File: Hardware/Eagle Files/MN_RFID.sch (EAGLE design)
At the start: 23 parts, among them IC1 74HCT125N, J1 USB_B_PTH, U1 ARGON

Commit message: Updated Schematic
Updated schematic per testing breadboard at MN 8/07/19.  Decided to power from Argon and remove external 5v USB connector, 3.3v power converter, and 100 uF cap.  5v supplied from Argon via VUSB pin.  3.3v supplied from Argon via 3.3v pin.  Also added 5.6Kohm pulldown on D4 to prevent buzzer from going off while Argon sets up.
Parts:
- removed C3: 100uF, adafruit:CPOL-USE2.5-5
- removed J1: USB_B_PTH, SparkFun-Connectors:USB_B_PTH
- removed PWR: (no value), adafruit:PINHD-1X3
- added R7: 5.6k, adafruit:R-US_0204/7
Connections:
- removed net N$19: IC1A.I, U1.D2
- new net N$22: IC1A.I, R7.1, U1.D2
- net 3.3V: no longer PWR.2
- net 5V: now also U1.VUSB; no longer C3.+, J1.VBUS, PWR.1
- net GND: now also R7.2; no longer C3.-, J1.GND, J1.SHIELD, PWR.3
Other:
- note added: "N/C"
- note removed: "OUT"
- note removed: "VIN"

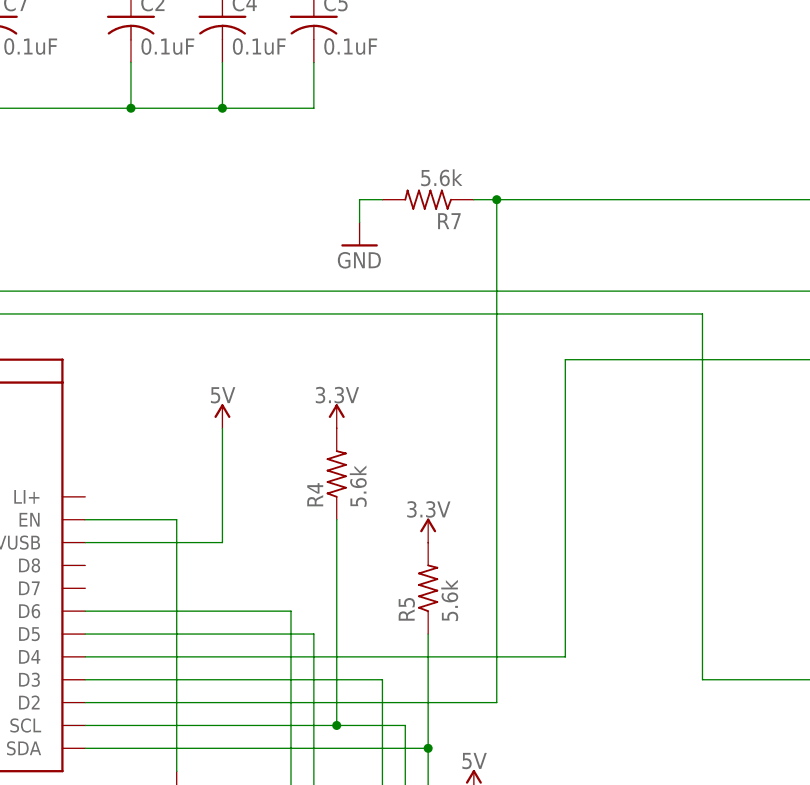
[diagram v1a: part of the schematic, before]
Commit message: Updated schematic
Changed pull-up/down resistors from 5.6K to 4.7K -- more common value.
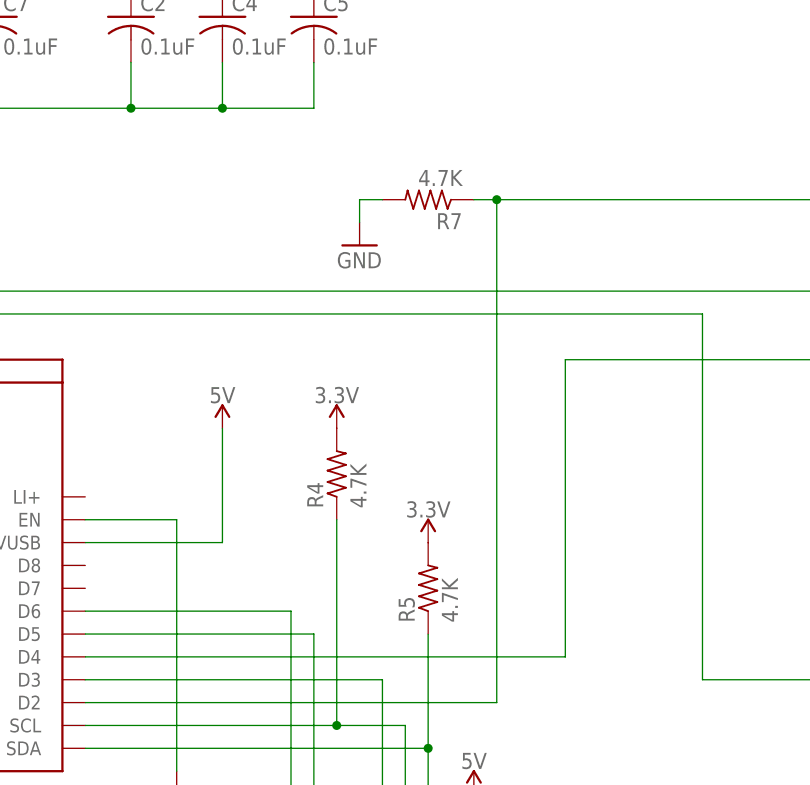
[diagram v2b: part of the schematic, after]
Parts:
- R4, R5, R7: value 5.6k -> 4.7K
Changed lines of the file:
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@@
 <part name="SUPPLY7" library="SparkFun-PowerSymbols" library_urn="urn:adsk.eagle:library:530" deviceset="5V" device=""/>
 <part name="GND9" library="supply1" library_urn="urn:adsk.eagle:library:371" deviceset="GND" device=""/>
-<part name="R4" library="adafruit" library_urn="urn:adsk.eagle:library:420" deviceset="R-US_" device="0204/7" package3d_urn="urn:adsk.eagle:package:6240596/1" value="5.6k"/>
-<part name="R5" library="adafruit" library_urn="urn:adsk.eagle:library:420" deviceset="R-US_" device="0204/7" package3d_urn="urn:adsk.eagle:package:6240596/1" value="5.6k"/>
+<part name="R4" library="adafruit" library_urn="urn:adsk.eagle:library:420" deviceset="R-US_" device="0204/7" package3d_urn="urn:adsk.eagle:package:6240596/1" value="4.7K"/>
+<part name="R5" library="adafruit" library_urn="urn:adsk.eagle:library:420" deviceset="R-US_" device="0204/7" package3d_urn="urn:adsk.eagle:package:6240596/1" value="4.7K"/>
 <part name="SUPPLY6" library="SparkFun-PowerSymbols" library_urn="urn:adsk.eagle:library:530" deviceset="3.3V" device=""/>
 <part name="SUPPLY8" library="SparkFun-PowerSymbols" library_urn="urn:adsk.eagle:library:530" deviceset="3.3V" device=""/>
@@
 <part name="C7" library="adafruit" library_urn="urn:adsk.eagle:library:420" deviceset="C-US" device="025-024X044" package3d_urn="urn:adsk.eagle:package:6240324/1" value="0.1uF"/>
 <part name="SUPPLY11" library="SparkFun-PowerSymbols" library_urn="urn:adsk.eagle:library:530" deviceset="5V" device=""/>
-<part name="R7" library="adafruit" library_urn="urn:adsk.eagle:library:420" deviceset="R-US_" device="0204/7" package3d_urn="urn:adsk.eagle:package:6240596/1" value="5.6k"/>
+<part name="R7" library="adafruit" library_urn="urn:adsk.eagle:library:420" deviceset="R-US_" device="0204/7" package3d_urn="urn:adsk.eagle:package:6240596/1" value="4.7K"/>
 <part name="GND11" library="supply1" library_urn="urn:adsk.eagle:library:371" deviceset="GND" device=""/>
 </parts>

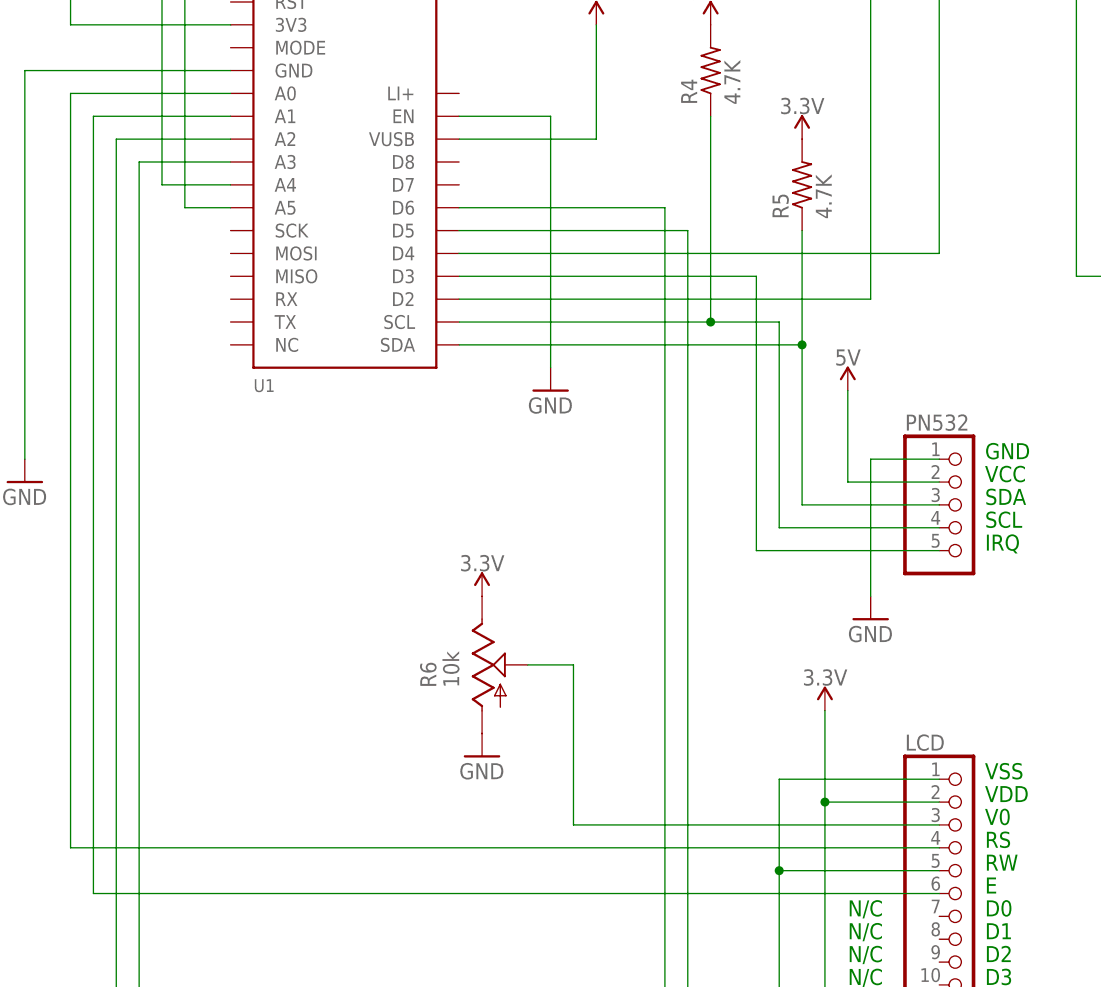
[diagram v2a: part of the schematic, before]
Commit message: PCB Finalization
Added expansion connector and board name.  Routed and coppoer pour.  Annotated the top silkscreen layer for connection information.
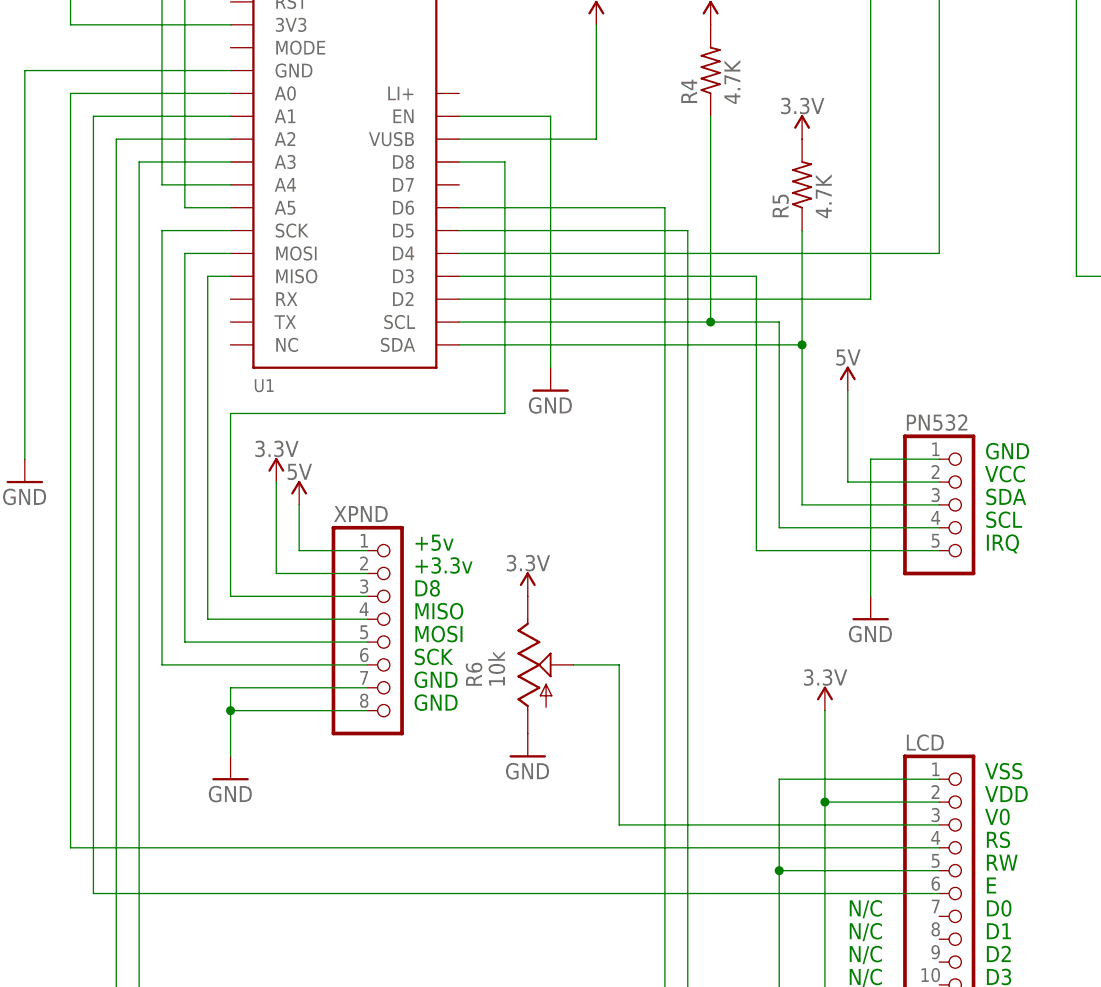
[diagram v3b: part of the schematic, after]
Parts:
- added XPND: (no value), adafruit:PINHD-1X8BIG
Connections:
- new net N$19: U1.D8, XPND.3
- new net N$23: U1.MISO, XPND.4
- new net N$24: U1.MOSI, XPND.5
- new net N$25: U1.SCK, XPND.6
- net 3.3V: now also XPND.2
- net 5V: now also XPND.1
- net GND: now also XPND.7, XPND.8
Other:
- note added: "+3.3v"
- note added: "+5v"
- note added: "D8"
- note added: "MISO"
- note added: "MOSI"
- note added: "SCK"
- moved on the sheet: R6
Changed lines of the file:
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@@
 <part name="R7" library="adafruit" library_urn="urn:adsk.eagle:library:420" deviceset="R-US_" device="0204/7" package3d_urn="urn:adsk.eagle:package:6240596/1" value="4.7K"/>
 <part name="GND11" library="supply1" library_urn="urn:adsk.eagle:library:371" deviceset="GND" device=""/>
+<part name="XPND" library="adafruit" library_urn="urn:adsk.eagle:library:420" deviceset="PINHD-1X8" device="BIG" package3d_urn="urn:adsk.eagle:package:6240707/1"/>
+<part name="SUPPLY10" library="SparkFun-PowerSymbols" library_urn="urn:adsk.eagle:library:530" deviceset="5V" device=""/>
+<part name="SUPPLY12" library="SparkFun-PowerSymbols" library_urn="urn:adsk.eagle:library:530" deviceset="3.3V" device=""/>
+<part name="GND12" library="supply1" library_urn="urn:adsk.eagle:library:371" deviceset="GND" device=""/>
 </parts>
 <sheets>
@@
 <text x="-38.1" y="15.24" size="1.778" layer="91">N/C</text>
 <text x="-38.1" y="12.7" size="1.778" layer="91">N/C</text>
+<text x="-86.36" y="60.96" size="1.778" layer="91">+5v</text>
+<text x="-86.36" y="58.42" size="1.778" layer="91">+3.3v</text>
+<text x="-86.36" y="55.88" size="1.778" layer="91">D8</text>
+<text x="-86.36" y="53.34" size="1.778" layer="91">MISO</text>
+<text x="-86.36" y="50.8" size="1.778" layer="91">MOSI</text>
+<text x="-86.36" y="48.26" size="1.778" layer="91">SCK</text>
+<text x="-86.36" y="45.72" size="1.778" layer="91">GND</text>
+<text x="-86.36" y="43.18" size="1.778" layer="91">GND</text>
 </plain>
 <instances>
@@
 <attribute name="VALUE" x="-100.584" y="160.909" size="1.778" layer="96"/>
 </instance>
-<instance part="R6" gate="G$1" x="-78.74" y="48.26" smashed="yes">
-<attribute name="NAME" x="-83.82" y="45.72" size="1.778" layer="95" rot="R90"/>
-<attribute name="VALUE" x="-81.28" y="45.72" size="1.778" layer="96" rot="R90"/>
-</instance>
-<instance part="GND10" gate="1" x="-78.74" y="38.1" smashed="yes">
-<attribute name="VALUE" x="-81.28" y="35.56" size="1.778" layer="96"/>
-</instance>
-<instance part="SUPPLY9" gate="G$1" x="-78.74" y="55.88" smashed="yes">
-<attribute name="VALUE" x="-78.74" y="58.674" size="1.778" layer="96" align="bottom-center"/>
+<instance part="R6" gate="G$1" x="-73.66" y="48.26" smashed="yes">
+<attribute name="NAME" x="-78.74" y="45.72" size="1.778" layer="95" rot="R90"/>
+<attribute name="VALUE" x="-76.2" y="45.72" size="1.778" layer="96" rot="R90"/>
+</instance>
+<instance part="GND10" gate="1" x="-73.66" y="38.1" smashed="yes">
+<attribute name="VALUE" x="-76.2" y="35.56" size="1.778" layer="96"/>
+</instance>
+<instance part="SUPPLY9" gate="G$1" x="-73.66" y="55.88" smashed="yes">
+<attribute name="VALUE" x="-73.66" y="58.674" size="1.778" layer="96" align="bottom-center"/>
 </instance>
 <instance part="C7" gate="G$1" x="-91.44" y="165.1" smashed="yes">
@@
 <instance part="GND11" gate="1" x="-50.8" y="139.7" smashed="yes">
 <attribute name="VALUE" x="-53.34" y="137.16" size="1.778" layer="96"/>
+</instance>
+<instance part="XPND" gate="G$1" x="-88.9" y="53.34" smashed="yes">
+<attribute name="NAME" x="-95.25" y="64.135" size="1.778" layer="95"/>
+<attribute name="VALUE" x="-95.25" y="38.1" size="1.778" layer="96"/>
+</instance>
+<instance part="SUPPLY10" gate="G$1" x="-99.06" y="66.04" smashed="yes">
+<attribute name="VALUE" x="-99.06" y="68.834" size="1.778" layer="96" align="bottom-center"/>
+</instance>
+<instance part="SUPPLY12" gate="G$1" x="-101.6" y="68.58" smashed="yes">
+<attribute name="VALUE" x="-101.6" y="71.374" size="1.778" layer="96" align="bottom-center"/>
+</instance>
+<instance part="GND12" gate="1" x="-106.68" y="35.56" smashed="yes">
+<attribute name="VALUE" x="-109.22" y="33.02" size="1.778" layer="96"/>
 </instance>
 </instances>
@@
 <wire x1="-50.8" y1="144.78" x2="-50.8" y2="142.24" width="0.1524" layer="91"/>
 </segment>
+<segment>
+<pinref part="XPND" gate="G$1" pin="7"/>
+<wire x1="-91.44" y1="45.72" x2="-106.68" y2="45.72" width="0.1524" layer="91"/>
+<pinref part="GND12" gate="1" pin="GND"/>
+<wire x1="-106.68" y1="45.72" x2="-106.68" y2="43.18" width="0.1524" layer="91"/>
+<pinref part="XPND" gate="G$1" pin="8"/>
+<wire x1="-106.68" y1="43.18" x2="-106.68" y2="38.1" width="0.1524" layer="91"/>
+<wire x1="-91.44" y1="43.18" x2="-106.68" y2="43.18" width="0.1524" layer="91"/>
+<junction x="-106.68" y="43.18"/>
+</segment>
 </net>
 <net name="N$1" class="0">
@@
 <wire x1="-66.04" y1="106.68" x2="-81.28" y2="106.68" width="0.1524" layer="91"/>
 </segment>
+<segment>
+<pinref part="SUPPLY10" gate="G$1" pin="5V"/>
+<wire x1="-99.06" y1="66.04" x2="-99.06" y2="60.96" width="0.1524" layer="91"/>
+<pinref part="XPND" gate="G$1" pin="1"/>
+<wire x1="-99.06" y1="60.96" x2="-91.44" y2="60.96" width="0.1524" layer="91"/>
+</segment>
 </net>
 <net name="3.3V" class="0">
@@
 <wire x1="-43.18" y1="175.26" x2="-43.18" y2="180.34" width="0.1524" layer="91"/>
 </segment>
+<segment>
+<pinref part="SUPPLY12" gate="G$1" pin="3.3V"/>
+<wire x1="-101.6" y1="68.58" x2="-101.6" y2="58.42" width="0.1524" layer="91"/>
+<pinref part="XPND" gate="G$1" pin="2"/>
+<wire x1="-101.6" y1="58.42" x2="-91.44" y2="58.42" width="0.1524" layer="91"/>
+</segment>
 </net>
 <net name="N$2" class="0">
@@
 <net name="N$17" class="0">
 <segment>
+<pinref part="LCD" gate="A" pin="3"/>
+<wire x1="-27.94" y1="30.48" x2="-63.5" y2="30.48" width="0.1524" layer="91"/>
 <pinref part="R6" gate="G$1" pin="S"/>
-<wire x1="-68.58" y1="30.48" x2="-68.58" y2="48.26" width="0.1524" layer="91"/>
-<wire x1="-68.58" y1="48.26" x2="-73.66" y2="48.26" width="0.1524" layer="91"/>
-<pinref part="LCD" gate="A" pin="3"/>
-<wire x1="-27.94" y1="30.48" x2="-68.58" y2="30.48" width="0.1524" layer="91"/>
+<wire x1="-68.58" y1="48.26" x2="-63.5" y2="48.26" width="0.1524" layer="91"/>
+<wire x1="-63.5" y1="48.26" x2="-63.5" y2="30.48" width="0.1524" layer="91"/>
 </segment>
 </net>
@@
 </segment>
 </net>
+<net name="N$19" class="0">
+<segment>
+<pinref part="U1" gate="U1" pin="D8"/>
+<wire x1="-81.28" y1="104.14" x2="-76.2" y2="104.14" width="0.1524" layer="91"/>
+<wire x1="-76.2" y1="104.14" x2="-76.2" y2="76.2" width="0.1524" layer="91"/>
+<wire x1="-76.2" y1="76.2" x2="-106.68" y2="76.2" width="0.1524" layer="91"/>
+<wire x1="-106.68" y1="76.2" x2="-106.68" y2="55.88" width="0.1524" layer="91"/>
+<pinref part="XPND" gate="G$1" pin="3"/>
+<wire x1="-106.68" y1="55.88" x2="-91.44" y2="55.88" width="0.1524" layer="91"/>
+</segment>
+</net>
+<net name="N$23" class="0">
+<segment>
+<pinref part="U1" gate="U1" pin="MISO"/>
+<wire x1="-106.68" y1="91.44" x2="-109.22" y2="91.44" width="0.1524" layer="91"/>
+<pinref part="XPND" gate="G$1" pin="4"/>
+<wire x1="-109.22" y1="91.44" x2="-109.22" y2="53.34" width="0.1524" layer="91"/>
+<wire x1="-109.22" y1="53.34" x2="-91.44" y2="53.34" width="0.1524" layer="91"/>
+</segment>
+</net>
+<net name="N$24" class="0">
+<segment>
+<pinref part="U1" gate="U1" pin="MOSI"/>
+<wire x1="-106.68" y1="93.98" x2="-111.76" y2="93.98" width="0.1524" layer="91"/>
+<wire x1="-111.76" y1="93.98" x2="-111.76" y2="50.8" width="0.1524" layer="91"/>
+<pinref part="XPND" gate="G$1" pin="5"/>
+<wire x1="-111.76" y1="50.8" x2="-91.44" y2="50.8" width="0.1524" layer="91"/>
+</segment>
+</net>
+<net name="N$25" class="0">
+<segment>
+<pinref part="U1" gate="U1" pin="SCK"/>
+<wire x1="-106.68" y1="96.52" x2="-114.3" y2="96.52" width="0.1524" layer="91"/>
+<wire x1="-114.3" y1="96.52" x2="-114.3" y2="48.26" width="0.1524" layer="91"/>
+<pinref part="XPND" gate="G$1" pin="6"/>
+<wire x1="-114.3" y1="48.26" x2="-91.44" y2="48.26" width="0.1524" layer="91"/>
+</segment>
+</net>
